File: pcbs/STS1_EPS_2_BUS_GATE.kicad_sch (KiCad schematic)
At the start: 17 parts, among them Q5 SI7135DP-T1-GE3, Q6 2N7002, U13 4082, U3 TPS2420RSAT

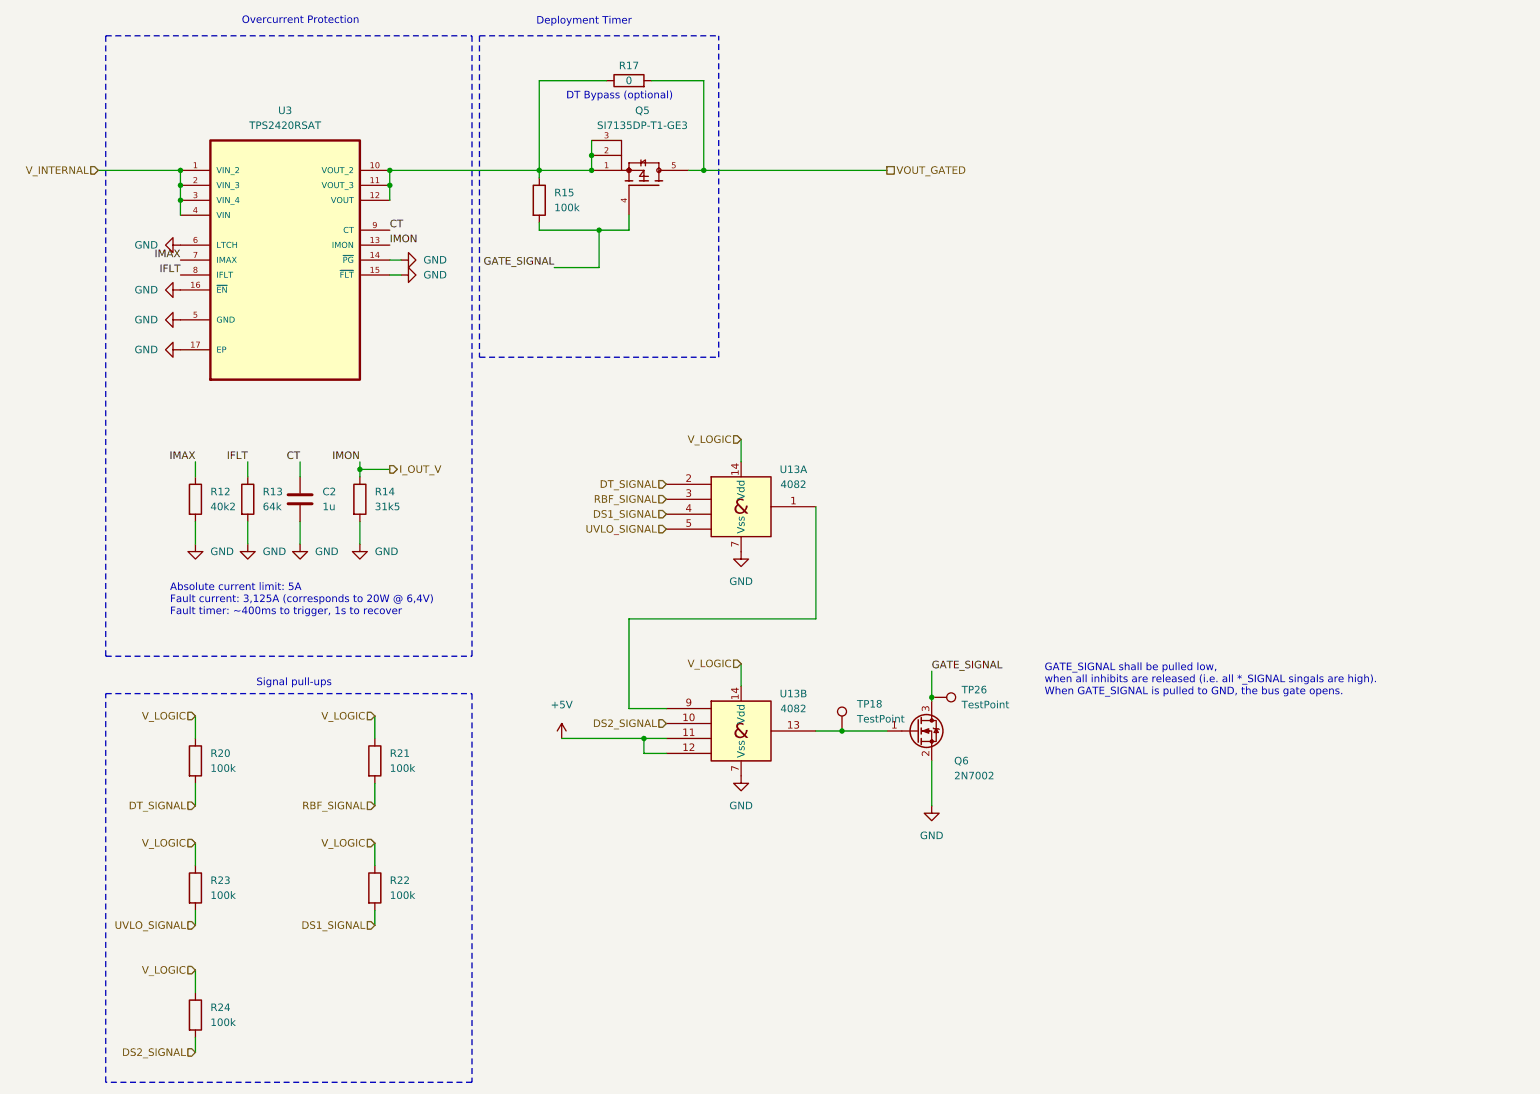
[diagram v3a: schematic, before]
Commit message: Removed UCI connector from STS1_EPS_2 and merged UCI connector with J5 on STS1_EPS_1.
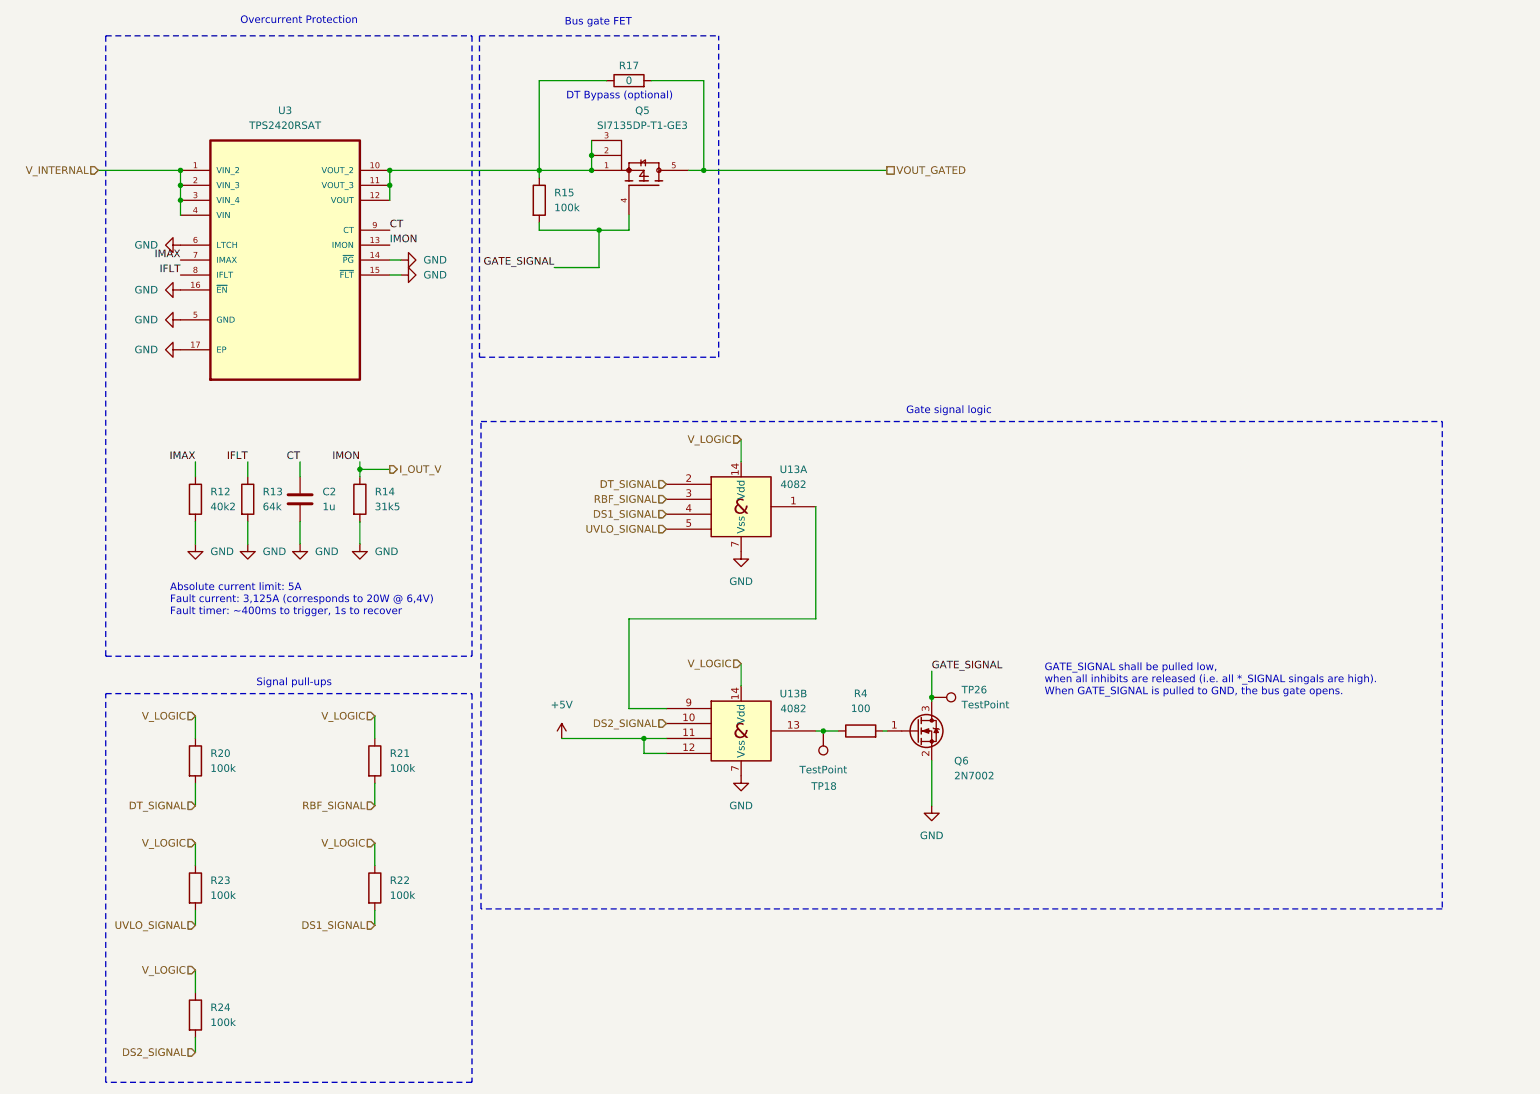
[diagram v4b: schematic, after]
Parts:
- added R4: 100, Resistor_SMD:R_0805_2012Metric, symbol Device:R
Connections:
- net at TP18.1, U13.13: now also R4.1; no longer Q6.1 (G)
- new net: Q6.1 (G), R4.2
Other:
- note added: "Bus gate FET"
- note added: "Gate signal logic"
- note removed: "Deployment Timer"
- moved on the sheet: TP18
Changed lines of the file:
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@@
-	)
-	(junction
-		(at 153.035 134.62)
-		(diameter 0)
-		(color 0 0 0 0)
 	)
 	(junction
@@
 	)
 	(junction
+		(at 149.86 134.62)
+		(diameter 0)
+		(color 0 0 0 0)
+	)
+	(junction
 		(at 110.49 36.83)
 		(diameter 0)
@@
 	(wire
 		(pts
+			(xy 149.86 134.62) (xy 152.4 134.62)
+		)
+		(stroke
+			(width 0)
+			(type default)
+		)
+	)
+	(wire
+		(pts
 			(xy 73.66 165.1) (xy 73.66 167.64)
 		)
@@
 	(wire
 		(pts
+			(xy 160.02 134.62) (xy 160.655 134.62)
+		)
+		(stroke
+			(width 0)
+			(type default)
+		)
+	)
+	(wire
+		(pts
 			(xy 26.67 39.37) (xy 40.64 39.37)
 		)
@@
 	(wire
 		(pts
-			(xy 153.035 134.62) (xy 160.655 134.62)
-		)
-		(stroke
-			(width 0)
-			(type default)
-		)
-	)
-	(wire
-		(pts
 			(xy 168.275 139.7) (xy 168.275 147.32)
 		)
@@
 	(wire
 		(pts
-			(xy 148.59 134.62) (xy 153.035 134.62)
+			(xy 148.59 134.62) (xy 149.86 134.62)
 		)
 		(stroke
@@
 		)
 	)
+	(rectangle
+		(start 91.694 82.042)
+		(end 255.016 164.846)
+		(stroke
+			(width 0)
+			(type dash)
+		)
+		(fill
+			(type none)
+		)
+	)
 	(text "Signal pull-ups"
 		(exclude_from_sim no)
@@
 		)
 	)
+	(text "Gate signal logic"
+		(exclude_from_sim no)
+		(at 171.196 80.264 0)
+		(effects
+			(font
+				(size 1.27 1.27)
+			)
+		)
+	)
 	(text "Overcurrent Protection\n"
 		(exclude_from_sim no)
-		(at 51.054 14.732 0)
+		(at 50.8 14.732 0)
 		(effects
 			(font
@@
 		)
 	)
-	(text "Deployment Timer"
-		(exclude_from_sim no)
-		(at 101.092 14.8336 0)
+	(text "Bus gate FET"
+		(exclude_from_sim no)
+		(at 105.918 14.986 0)
 		(effects
 			(font
@@
 	(symbol
 		(lib_id "Connector:TestPoint")
-		(at 153.035 134.62 0)
+		(at 149.86 134.62 180)
 		(unit 1)
 		(exclude_from_sim no)
@@
 		(on_board yes)
 		(dnp no)
-		(fields_autoplaced yes)
 		(property "Reference" "TP18"
-			(at 155.575 130.0479 0)
+			(at 152.146 144.018 0)
 			(effects
 				(font
@@
 		)
 		(property "Value" "TestPoint"
-			(at 155.575 132.5879 0)
+			(at 153.924 141.224 0)
 			(effects
 				(font
@@
 		)
 		(property "Footprint" "TestPoint:TestPoint_THTPad_D1.0mm_Drill0.5mm"
-			(at 158.115 134.62 0)
+			(at 144.78 134.62 0)
 			(effects
 				(font
@@
 		)
 		(property "Datasheet" "~"
-			(at 158.115 134.62 0)
+			(at 144.78 134.62 0)
 			(effects
 				(font
@@
 		)
 		(property "Description" ""
-			(at 153.035 134.62 0)
+			(at 149.86 134.62 0)
 			(effects
 				(font
@@
 					(unit 1)
 				)
+			)
+		)
+	)
+	(symbol
+		(lib_id "Device:R")
+		(at 156.21 134.62 90)
+		(unit 1)
+		(exclude_from_sim no)
+		(in_bom yes)
+		(on_board yes)
+		(dnp no)
+		(fields_autoplaced yes)
+		(property "Reference" "R4"
+			(at 156.21 128.27 90)
+			(effects
+				(font
+					(size 1.27 1.27)
+				)
+			)
+		)
+		(property "Value" "100"
+			(at 156.21 130.81 90)
+			(effects
+				(font
+					(size 1.27 1.27)
+				)
+			)
+		)
+		(property "Footprint" "Resistor_SMD:R_0805_2012Metric"
+			(at 156.21 136.398 90)
+			(effects
+				(font
+					(size 1.27 1.27)
+				)
+				(hide yes)
+			)
+		)
+		(property "Datasheet" "~"
+			(at 156.21 134.62 0)
+			(effects
+				(font
+					(size 1.27 1.27)
+				)
+				(hide yes)
+			)
+		)
+		(property "Description" "Resistor"
+			(at 156.21 134.62 0)
+			(effects
+				(font
+					(size 1.27 1.27)
+				)
+				(hide yes)
+			)
+		)
+		(pin "1"
+		)
+		(pin "2"
+		)
+		(instances
+			(project "STS1_EPS_2"
+				(path "/38c03ff7-ea47-4d00-b37d-ddcaa7d87722/4a4cf4f3-b3ca-46d9-b2ff-f21a8c4df335"
+					(reference "R4")
+					(unit 1)
+				)

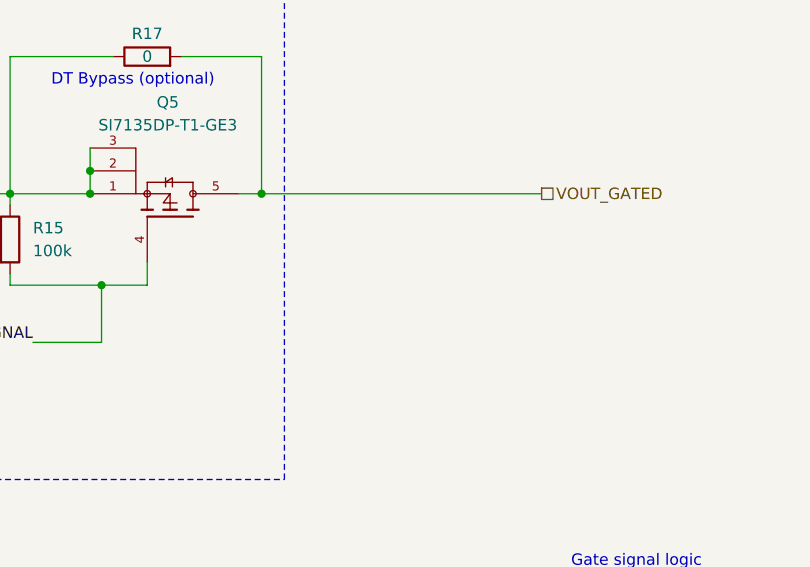
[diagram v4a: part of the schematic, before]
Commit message: Added even more ESD protection.
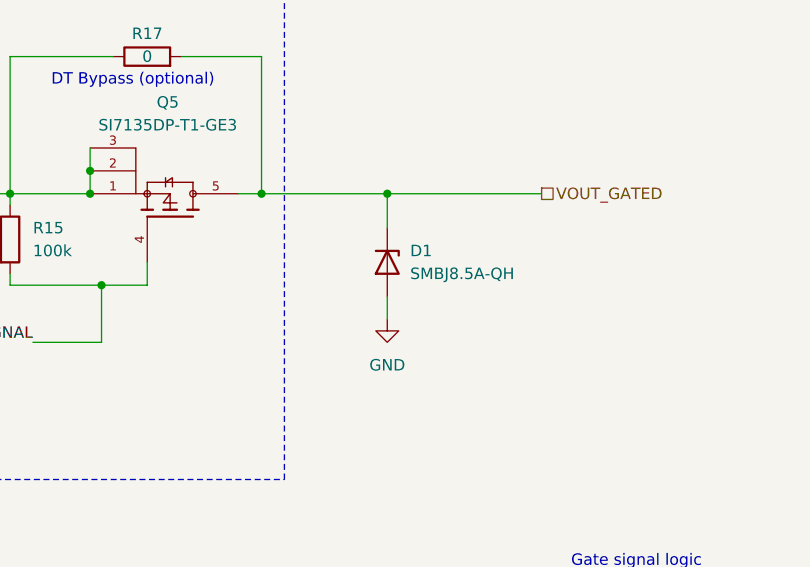
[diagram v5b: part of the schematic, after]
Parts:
- added D1: SMBJ8.5A-QH, Diode_SMD:D_SMB, symbol Diode:PTVS5V0Z1USK
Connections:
- net GND: now also D1.2 (A)
- net VOUT_GATED: now also D1.1 (K)
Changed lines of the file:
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@@
+	)
+	(junction
+		(at 143.51 39.37)
+		(diameter 0)
+		(color 0 0 0 0)
 	)
 	(junction
@@
 	(wire
 		(pts
+			(xy 143.51 39.37) (xy 143.51 43.18)
+		)
+		(stroke
+			(width 0)
+			(type default)
+		)
+	)
+	(wire
+		(pts
 			(xy 73.66 165.1) (xy 73.66 167.64)
 		)
@@
 		)
 	)
+	(wire
+		(pts
+			(xy 143.51 39.37) (xy 160.655 39.37)
+		)
+		(stroke
+			(width 0)
+			(type default)
+		)
+	)
 	(polyline
 		(pts
@@
 	(wire
 		(pts
+			(xy 143.51 50.8) (xy 143.51 53.34)
+		)
+		(stroke
+			(width 0)
+			(type default)
+		)
+	)
+	(wire
+		(pts
 			(xy 116.84 49.53) (xy 116.84 46.99)
 		)
@@
 	(wire
 		(pts
-			(xy 129.54 39.37) (xy 160.655 39.37)
+			(xy 129.54 39.37) (xy 143.51 39.37)
 		)
 		(stroke
@@
 					(unit 1)
 				)
+			)
+		)
+	)
+	(symbol
+		(lib_id "power:GND")
+		(at 143.51 53.34 0)
+		(unit 1)
+		(exclude_from_sim no)
+		(in_bom yes)
+		(on_board yes)
+		(dnp no)
+		(fields_autoplaced yes)
+		(property "Reference" "#PWR05"
+			(at 143.51 59.69 0)
+			(effects
+				(font
+					(size 1.27 1.27)
+				)
+				(hide yes)
+			)
+		)
+		(property "Value" "GND"
+			(at 143.51 58.42 0)
+			(effects
+				(font
+					(size 1.27 1.27)
+				)
+			)
+		)
+		(property "Footprint" ""
+			(at 143.51 53.34 0)
+			(effects
+				(font
+					(size 1.27 1.27)
+				)
+				(hide yes)
+			)
+		)
+		(property "Datasheet" ""
+			(at 143.51 53.34 0)
+			(effects
+				(font
+					(size 1.27 1.27)
+				)
+				(hide yes)
+			)
+		)
+		(property "Description" ""
+			(at 143.51 53.34 0)
+			(effects
+				(font
+					(size 1.27 1.27)
+				)
+				(hide yes)
+			)
+		)
+		(pin "1"
+		)
+		(instances
+			(project "STS1_EPS_2"
+				(path "/38c03ff7-ea47-4d00-b37d-ddcaa7d87722/4a4cf4f3-b3ca-46d9-b2ff-f21a8c4df335"
+					(reference "#PWR05")
+					(unit 1)
+				)
+			)
+		)
+	)
+	(symbol
+		(lib_id "Diode:PTVS5V0Z1USK")
+		(at 143.51 46.99 270)
+		(unit 1)
+		(exclude_from_sim no)
+		(in_bom yes)
+		(on_board yes)
+		(dnp no)
+		(fields_autoplaced yes)
+		(property "Reference" "D1"
+			(at 146.05 45.7199 90)
+			(effects
+				(font
+					(size 1.27 1.27)
+				)
+				(justify left)
+			)
+		)
+		(property "Value" "SMBJ8.5A-QH"
+			(at 146.05 48.2599 90)
+			(effects
+				(font
+					(size 1.27 1.27)
+				)
+				(justify left)
+			)
+		)
+		(property "Footprint" "Diode_SMD:D_SMB"
+			(at 139.065 46.99 0)
+			(effects
+				(font
+					(size 1.27 1.27)
+				)
+				(hide yes)
+			)
+		)
+		(property "Datasheet" ""
+			(at 143.51 46.99 0)
+			(effects
+				(font
+					(size 1.27 1.27)
+				)
+				(hide yes)
+			)
+		)
+		(property "Description" ""
+			(at 143.51 46.99 0)
+			(effects
+				(font
+					(size 1.27 1.27)
+				)
+				(hide yes)
+			)
+		)
+		(pin "1"
+		)
+		(pin "2"
+		)
+		(instances
+			(project "STS1_EPS_2"
+				(path "/38c03ff7-ea47-4d00-b37d-ddcaa7d87722/4a4cf4f3-b3ca-46d9-b2ff-f21a8c4df335"
+					(reference "D1")
+					(unit 1)
+				)
